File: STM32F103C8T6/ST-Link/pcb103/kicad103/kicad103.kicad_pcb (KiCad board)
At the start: 4 copper layers, 82 x 52 mm, 32 parts, among them IC1 LD1117DT33TR, J1 0480372200, J2 Conn_01x02_Socket, J3 Conn_02x05_Odd_Even, J5 Conn_01x16_Pin, J7 Conn_01x04_Pin, J8 Conn_01x05_Socket, J9 Conn_01x17_Pin, U1 STM32F103C8T6, Y1 8MHz 20pF

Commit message: Fix remaining
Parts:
- moved C6 0.80 mm to (81.6, 60.2)
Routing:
- net +3.3V: track 50.2 -> 51.9 mm
- net PA15: track 85.7 -> 87.0 mm

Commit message: Move line from top header
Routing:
- net PB11: track 65.7 -> 67.9 mm
- net PB14: track 98.2 -> 100.2 mm
- net PB13: track 88.4 -> 86.5 mm, vias 1 -> 3

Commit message: Move out bottom lines
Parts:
- moved H4 1.10 mm to (56.6, 87.0)
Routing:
- net PB0: track 115.9 -> 99.9 mm
- net PB1: track 124.3 -> 109.0 mm
- net PB2: track 122.5 -> 108.8 mm
- net PB15: track 122.3 -> 135.5 mm
- net PB10: track 128.0 -> 115.9 mm
- net PC15: track 76.8 -> 87.9 mm
- net PB11: track 67.9 -> 61.3 mm
- net PC13: track 79.3 -> 84.1 mm
- net PC14: track 38.6 -> 38.9 mm, vias 1 -> 3

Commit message: Move out mounting hole
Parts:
- removed H4: MountingHole_Pad, MountingHole:MountingHole_4.3mm_M4_Pad_Via
- moved H2 6.35 mm to (121.2, 88.2)
- moved H3 2.38 mm to (58.0, 50.6)
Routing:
- net PB10: track 115.9 -> 177.0 mm
- net PB2: track 108.8 -> 161.2 mm
- net PB1: track 109.0 -> 160.5 mm
- net PB0: track 99.9 -> 150.8 mm
- net PA1: track 24.1 -> 54.8 mm
- net PC15: track 87.9 -> 103.6 mm
- net PB15: track 135.5 -> 147.7 mm

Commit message: Clean lines from header pins
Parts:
- moved H1 7.08 mm to (121.2, 49.6)
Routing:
- net PA15: track 87.0 -> 102.2 mm
- net PB1: track 160.5 -> 154.6 mm, vias 3 -> 5
- net PB3: track 52.3 -> 47.2 mm
- net PB13: track 86.5 -> 91.4 mm
- net PB10: track 177.0 -> 172.5 mm
- net PB2: track 161.2 -> 157.1 mm
- net PB12: track 117.3 -> 120.9 mm
- net PB14: track 100.2 -> 98.8 mm
- net PA13: track 49.9 -> 51.3 mm
- net GND: track 44.2 -> 44.9 mm
- net PA14: track 61.9 -> 62.5 mm

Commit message: Add header 1 front lables
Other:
- board text added: "PA0"
- board text added: "PA1"
- board text added: "PA10"
- board text added: "PA13"
- board text added: "PA14"
- board text added: "PA15"
- board text added: "PA2"
- board text added: "PA3"
- board text added: "PA4"
- board text added: "PA5"
- board text added: "PA6"
- board text added: "PA7"
- board text added: "PA8"
- board text added: "PA9"
- board text added: "PC13"
- board text added: "PC14"
- board text added: "PC15"
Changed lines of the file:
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@@
     (effects (font (size 1 1) (thickness 0.2) bold) (justify left bottom mirror))
+  )
+  (gr_text "PC14" (at 105 92.9 90) (layer "F.SilkS")
+    (effects (font (size 1 1) (thickness 0.2) bold) (justify left bottom))
   )
   (gr_text "1" (at 95.1 59.5) (layer "F.SilkS")
@@
     (effects (font (size 1 1) (thickness 0.2) bold) (justify left bottom))
   )
+  (gr_text "PA13" (at 94.8 92.9 90) (layer "F.SilkS")
+    (effects (font (size 1 1) (thickness 0.2) bold) (justify left bottom))
+  )
+  (gr_text "PA1" (at 69.3 91.8 90) (layer "F.SilkS")
+    (effects (font (size 1 1) (thickness 0.2) bold) (justify left bottom))
+  )
   (gr_text "JTAG" (at 98.7 57.6) (layer "F.SilkS")
+    (effects (font (size 1 1) (thickness 0.2) bold) (justify left bottom))
+  )
+  (gr_text "PA5" (at 79.6 91.8 90) (layer "F.SilkS")
     (effects (font (size 1 1) (thickness 0.2) bold) (justify left bottom))
   )
@@
     (effects (font (size 1 1) (thickness 0.2) bold) (justify left bottom))
   )
+  (gr_text "PA2" (at 71.9 91.8 90) (layer "F.SilkS")
+    (effects (font (size 1 1) (thickness 0.2) bold) (justify left bottom))
+  )
   (gr_text "SWDIO" (at 110.5 64.3) (layer "F.SilkS")
     (effects (font (size 1 1) (thickness 0.2) bold) (justify left bottom))
   )
+  (gr_text "PC15" (at 107.5 92.9 90) (layer "F.SilkS")
+    (effects (font (size 1 1) (thickness 0.2) bold) (justify left bottom))
+  )
+  (gr_text "PA15" (at 99.9 92.9 90) (layer "F.SilkS")
+    (effects (font (size 1 1) (thickness 0.2) bold) (justify left bottom))
+  )
+  (gr_text "PA8" (at 87.2 91.8 90) (layer "F.SilkS")
+    (effects (font (size 1 1) (thickness 0.2) bold) (justify left bottom))
+  )
   (gr_text "SWCLK" (at 110.5 67) (layer "F.SilkS")
+    (effects (font (size 1 1) (thickness 0.2) bold) (justify left bottom))
+  )
+  (gr_text "PA0" (at 66.8 91.8 90) (layer "F.SilkS")
+    (effects (font (size 1 1) (thickness 0.2) bold) (justify left bottom))
+  )
+  (gr_text "1" (at 78.5 65.7) (layer "F.SilkS")
+    (effects (font (size 1 1) (thickness 0.2) bold) (justify left bottom))
+  )
+  (gr_text "PA4" (at 77 91.8 90) (layer "F.SilkS")
+    (effects (font (size 1 1) (thickness 0.2) bold) (justify left bottom))
+  )
+  (gr_text "PA10" (at 92.2 92.9 90) (layer "F.SilkS")
     (effects (font (size 1 1) (thickness 0.2) bold) (justify left bottom))
   )
@@
   )
   (gr_text "+" (at 64.2 76.1) (layer "F.SilkS")
+    (effects (font (size 1 1) (thickness 0.2) bold) (justify left bottom))
+  )
+  (gr_text "PA9" (at 89.7 91.8 90) (layer "F.SilkS")
+    (effects (font (size 1 1) (thickness 0.2) bold) (justify left bottom))
+  )
+  (gr_text "PA7" (at 84.7 91.8 90) (layer "F.SilkS")
+    (effects (font (size 1 1) (thickness 0.2) bold) (justify left bottom))
+  )
+  (gr_text "PA14" (at 97.3 92.9 90) (layer "F.SilkS")
+    (effects (font (size 1 1) (thickness 0.2) bold) (justify left bottom))
+  )
+  (gr_text "PA3" (at 74.4 91.8 90) (layer "F.SilkS")
     (effects (font (size 1 1) (thickness 0.2) bold) (justify left bottom))
   )
@@
     (effects (font (size 1 1) (thickness 0.2) bold) (justify left bottom))
   )
+  (gr_text "PC13" (at 102.4 92.9 90) (layer "F.SilkS")
+    (effects (font (size 1 1) (thickness 0.2) bold) (justify left bottom))
+  )
+  (gr_text "PA6" (at 82.2 91.8 90) (layer "F.SilkS")
+    (effects (font (size 1 1) (thickness 0.2) bold) (justify left bottom))
+  )

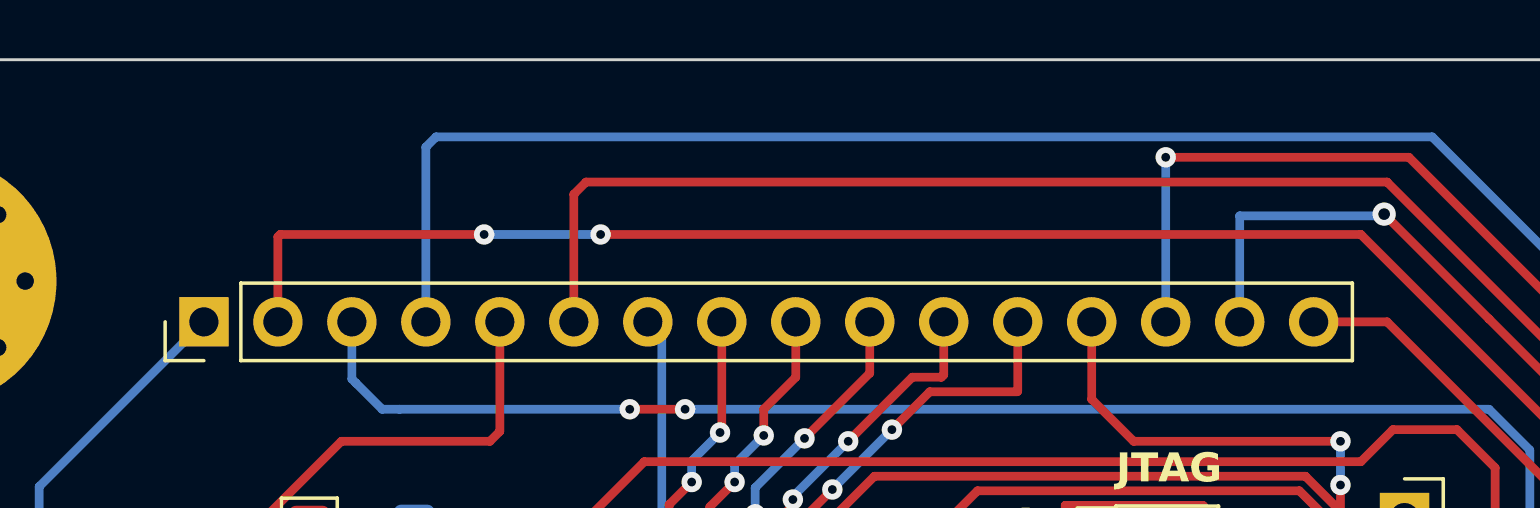
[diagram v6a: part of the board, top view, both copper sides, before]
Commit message: Add header 1 back lables
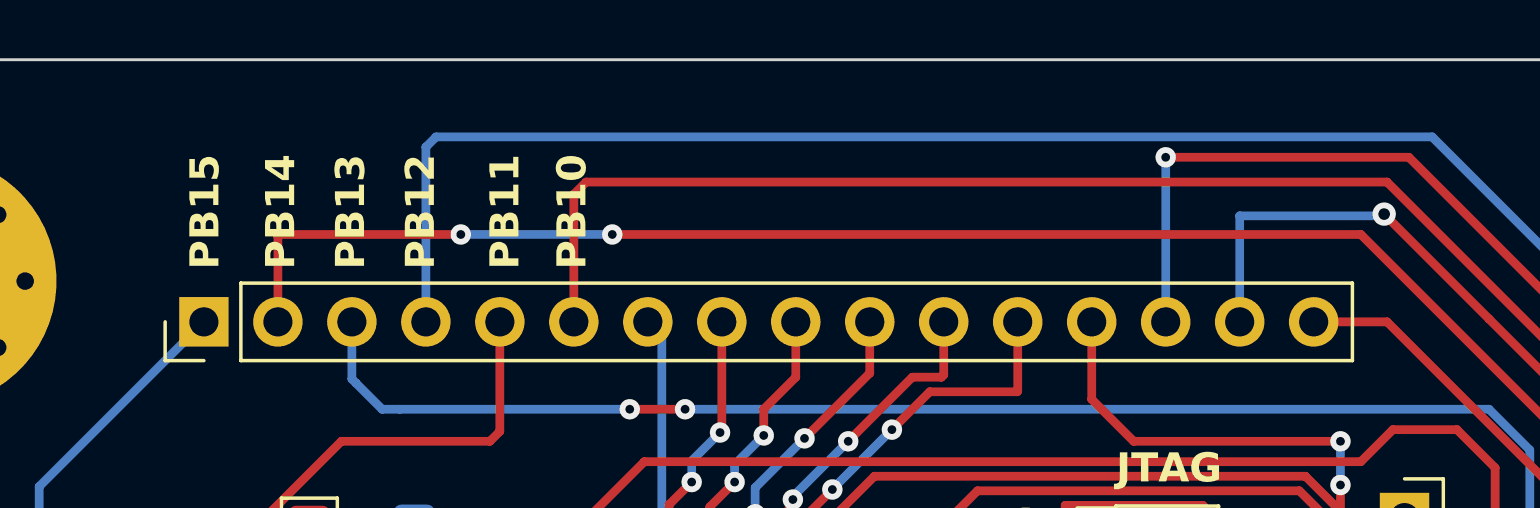
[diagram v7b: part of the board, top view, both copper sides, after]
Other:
- board text added: "PB10"
- board text added: "PB11"
- board text added: "PB12"
- board text added: "PB13"
- board text added: "PB14"
- board text added: "PB15"
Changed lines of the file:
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@@
   (gr_line (start 124 43) (end 58 43)
     (stroke (width 0.1) (type default)) (layer "Edge.Cuts"))
+  (gr_text "PA2" (at 72 89.2 90) (layer "B.SilkS")
+    (effects (font (size 1 1) (thickness 0.2) bold) (justify left bottom mirror))
+  )
   (gr_text "GND" (at 113.7 69.5) (layer "B.SilkS")
     (effects (font (size 1 1) (thickness 0.2) bold) (justify left bottom mirror))
@@
     (effects (font (size 1 1) (thickness 0.2) bold) (justify left bottom mirror))
   )
+  (gr_text "PA14" (at 97.4 89.2 90) (layer "B.SilkS")
+    (effects (font (size 1 1) (thickness 0.2) bold) (justify left bottom mirror))
+  )
+  (gr_text "PA9" (at 89.8 89.2 90) (layer "B.SilkS")
+    (effects (font (size 1 1) (thickness 0.2) bold) (justify left bottom mirror))
+  )
+  (gr_text "PA4" (at 77.1 89.2 90) (layer "B.SilkS")
+    (effects (font (size 1 1) (thickness 0.2) bold) (justify left bottom mirror))
+  )
   (gr_text "PWR" (at 60.1 81.2) (layer "B.SilkS")
     (effects (font (size 1 1) (thickness 0.2) bold) (justify left bottom mirror))
   )
+  (gr_text "PA13" (at 94.8 89.2 90) (layer "B.SilkS")
+    (effects (font (size 1 1) (thickness 0.2) bold) (justify left bottom mirror))
+  )
+  (gr_text "PA10" (at 92.3 89.2 90) (layer "B.SilkS")
+    (effects (font (size 1 1) (thickness 0.2) bold) (justify left bottom mirror))
+  )
   (gr_text "SWDIO" (at 115.3 64.3) (layer "B.SilkS")
     (effects (font (size 1 1) (thickness 0.2) bold) (justify left bottom mirror))
@@
     (effects (font (size 1 1) (thickness 0.2) bold) (justify left bottom mirror))
   )
+  (gr_text "PA15" (at 99.9 89.2 90) (layer "B.SilkS")
+    (effects (font (size 1 1) (thickness 0.2) bold) (justify left bottom mirror))
+  )
+  (gr_text "PA6" (at 82.1 89.2 90) (layer "B.SilkS")
+    (effects (font (size 1 1) (thickness 0.2) bold) (justify left bottom mirror))
+  )
   (gr_text "SWCLK" (at 121 76.9) (layer "B.SilkS")
     (effects (font (size 1 1) (thickness 0.2) bold) (justify left bottom mirror))
   )
+  (gr_text "PC13" (at 102.5 89.2 90) (layer "B.SilkS")
+    (effects (font (size 1 1) (thickness 0.2) bold) (justify left bottom mirror))
+  )
+  (gr_text "PC14" (at 105 89.2 90) (layer "B.SilkS")
+    (effects (font (size 1 1) (thickness 0.2) bold) (justify left bottom mirror))
+  )
+  (gr_text "PA0" (at 66.8 89.2 90) (layer "B.SilkS")
+    (effects (font (size 1 1) (thickness 0.2) bold) (justify left bottom mirror))
+  )
   (gr_text "3.3V" (at 115.1 61.9) (layer "B.SilkS")
     (effects (font (size 1 1) (thickness 0.2) bold) (justify left bottom mirror))
@@
     (effects (font (size 1 1) (thickness 0.2) bold) (justify left bottom mirror))
   )
+  (gr_text "PA1" (at 69.4 89.2 90) (layer "B.SilkS")
+    (effects (font (size 1 1) (thickness 0.2) bold) (justify left bottom mirror))
+  )
+  (gr_text "PA3" (at 74.5 89.2 90) (layer "B.SilkS")
+    (effects (font (size 1 1) (thickness 0.2) bold) (justify left bottom mirror))
+  )
+  (gr_text "PA8" (at 87.2 89.2 90) (layer "B.SilkS")
+    (effects (font (size 1 1) (thickness 0.2) bold) (justify left bottom mirror))
+  )
   (gr_text "Slave" (at 106.6 61.8 90) (layer "B.SilkS")
     (effects (font (size 1 1) (thickness 0.2) bold) (justify left bottom mirror))
   )
+  (gr_text "PA5" (at 79.6 89.2 90) (layer "B.SilkS")
+    (effects (font (size 1 1) (thickness 0.2) bold) (justify left bottom mirror))
+  )
+  (gr_text "PC15" (at 107.5 89.2 90) (layer "B.SilkS")
+    (effects (font (size 1 1) (thickness 0.2) bold) (justify left bottom mirror))
+  )
   (gr_text "-" (at 62.8 78.5) (layer "B.SilkS")
     (effects (font (size 1 1) (thickness 0.2) bold) (justify left bottom mirror))
   )
+  (gr_text "PA7" (at 84.7 89.2 90) (layer "B.SilkS")
+    (effects (font (size 1 1) (thickness 0.2) bold) (justify left bottom mirror))
+  )
   (gr_text "3.3V" (at 119.3 71.9) (layer "B.SilkS")
     (effects (font (size 1 1) (thickness 0.2) bold) (justify left bottom mirror))
@@
     (effects (font (size 1 1) (thickness 0.2) bold) (justify left bottom))
   )
+  (gr_text "PB14" (at 70.6 50.2 90) (layer "F.SilkS")
+    (effects (font (size 1 1) (thickness 0.2) bold) (justify left bottom))
+  )
   (gr_text "PA13" (at 94.8 92.9 90) (layer "F.SilkS")
     (effects (font (size 1 1) (thickness 0.2) bold) (justify left bottom))
@@
     (effects (font (size 1 1) (thickness 0.2) bold) (justify left bottom))
   )
+  (gr_text "PB10" (at 80.6 50.2 90) (layer "F.SilkS")
+    (effects (font (size 1 1) (thickness 0.2) bold) (justify left bottom))
+  )
   (gr_text "SWCLK" (at 110.5 67) (layer "F.SilkS")
     (effects (font (size 1 1) (thickness 0.2) bold) (justify left bottom))
@@
     (effects (font (size 1 1) (thickness 0.2) bold) (justify left bottom))
   )
+  (gr_text "PB13" (at 73 50.2 90) (layer "F.SilkS")
+    (effects (font (size 1 1) (thickness 0.2) bold) (justify left bottom))
+  )
   (gr_text "PA14" (at 97.3 92.9 90) (layer "F.SilkS")
     (effects (font (size 1 1) (thickness 0.2) bold) (justify left bottom))
@@
     (effects (font (size 1 1) (thickness 0.2) bold) (justify left bottom))
   )
+  (gr_text "PB15" (at 68 50.2 90) (layer "F.SilkS")
+    (effects (font (size 1 1) (thickness 0.2) bold) (justify left bottom))
+  )
   (gr_text "3.3V" (at 111.5 61.9) (layer "F.SilkS")
     (effects (font (size 1 1) (thickness 0.2) bold) (justify left bottom))
@@
     (effects (font (size 1 1) (thickness 0.2) bold) (justify left bottom))
   )
+  (gr_text "PB12" (at 75.4 50.2 90) (layer "F.SilkS")
+    (effects (font (size 1 1) (thickness 0.2) bold) (justify left bottom))
+  )
   (gr_text "PC13" (at 102.4 92.9 90) (layer "F.SilkS")
+    (effects (font (size 1 1) (thickness 0.2) bold) (justify left bottom))
+  )
+  (gr_text "PB11" (at 78.3 50.2 90) (layer "F.SilkS")
     (effects (font (size 1 1) (thickness 0.2) bold) (justify left bottom))
   )
@@
   (segment (start 91 68.8) (end 91 71.6) (width 0.3) (layer "B.Cu") (net 19))
   (segment (start 61.6 81.71005) (end 65.352082 77.957968) (width 0.3) (layer "B.Cu") (net 19))
-  (segment (start 107.1 49) (end 81 49) (width 0.3) (layer "F.Cu") (net 20))
+  (segment (start 118.7 70.3) (end 118.7 61.7) (width 0.3) (layer "F.Cu") (net 20))
   (segment (start 102.2625 69.9) (end 105.9 73.5375) (width 0.3) (layer "F.Cu") (net 20))
-  (segment (start 114.7 56.6) (end 107.1 49) (width 0.3) (layer "F.Cu") (net 20))
   (segment (start 114 73.62) (end 105.9825 73.62) (width 0.3) (layer "F.Cu") (net 20))
+  (segment (start 70 49) (end 76.2 49) (width 0.3) (layer "F.Cu") (net 20))
   (segment (start 69.92 49.08) (end 69.92 52) (width 0.3) (layer "F.Cu") (net 20))
   (segment (start 70 49) (end 69.92 49.08) (width 0.3) (layer "F.Cu") (net 20))
+  (segment (start 114.7 56.6) (end 107.1 49) (width 0.3) (layer "F.Cu") (net 20))
   (segment (start 105.9825 73.62) (end 105.9 73.5375) (width 0.3) (layer "F.Cu") (net 20))
   (segment (start 115.38 73.62) (end 118.7 70.3) (width 0.3) (layer "F.Cu") (net 20))
+  (segment (start 107.1 49) (end 81.4 49) (width 0.3) (layer "F.Cu") (net 20))
+  (segment (start 114 73.62) (end 115.38 73.62) (width 0.3) (layer "F.Cu") (net 20))
   (segment (start 118.7 61.7) (end 114.7 57.7) (width 0.3) (layer "F.Cu") (net 20))
   (segment (start 114.7 57.7) (end 114.7 56.6) (width 0.3) (layer "F.Cu") (net 20))
   (segment (start 106.0025 73.64) (end 105.9 73.5375) (width 0.5) (layer "F.Cu") (net 20))
-  (segment (start 77 49) (end 70 49) (width 0.3) (layer "F.Cu") (net 20))
-  (segment (start 118.7 70.3) (end 118.7 61.7) (width 0.3) (layer "F.Cu") (net 20))
   (segment (start 89.1625 69.9) (end 102.2625 69.9) (width 0.3) (layer "F.Cu") (net 20))
-  (segment (start 114 73.62) (end 115.38 73.62) (width 0.3) (layer "F.Cu") (net 20))
-  (via (at 77 49) (size 0.7) (drill 0.3) (layers "F.Cu" "B.Cu") (net 20))
-  (via (at 81 49) (size 0.7) (drill 0.3) (layers "F.Cu" "B.Cu") (net 20))
-  (segment (start 81 49) (end 77 49) (width 0.3) (layer "B.Cu") (net 20))
+  (via (at 76.2 49) (size 0.7) (drill 0.3) (layers "F.Cu" "B.Cu") (net 20))
+  (via (at 81.4 49) (size 0.7) (drill 0.3) (layers "F.Cu" "B.Cu") (net 20))
+  (segment (start 81.4 49) (end 76.2 49) (width 0.3) (layer "B.Cu") (net 20))
   (segment (start 109 75.55) (end 103.55 75.55) (width 0.3) (layer "F.Cu") (net 21))
   (segment (start 113.39 75.55) (end 109 75.55) (width 0.3) (layer "F.Cu") (net 21))

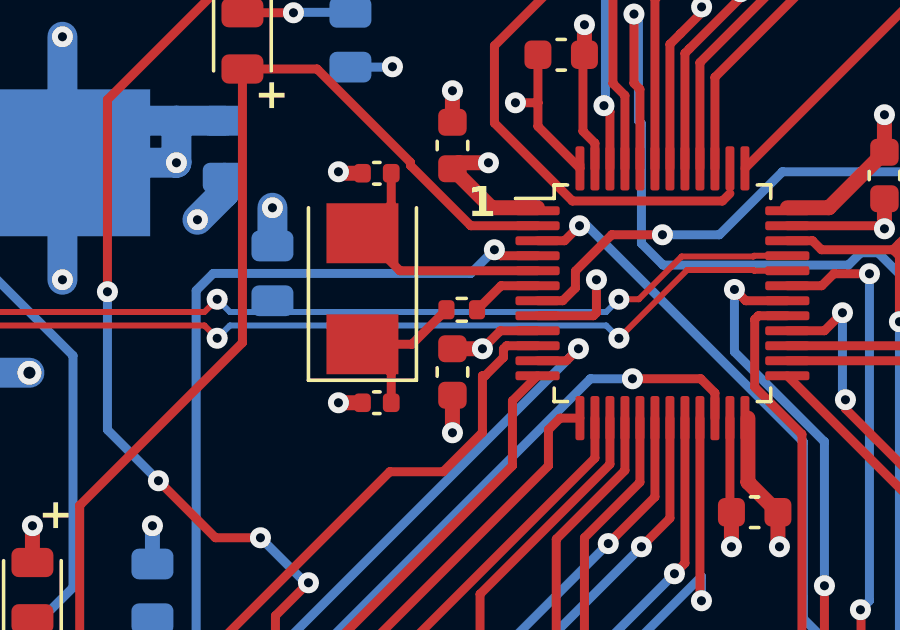
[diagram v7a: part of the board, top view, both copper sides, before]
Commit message: Move crystal resistor
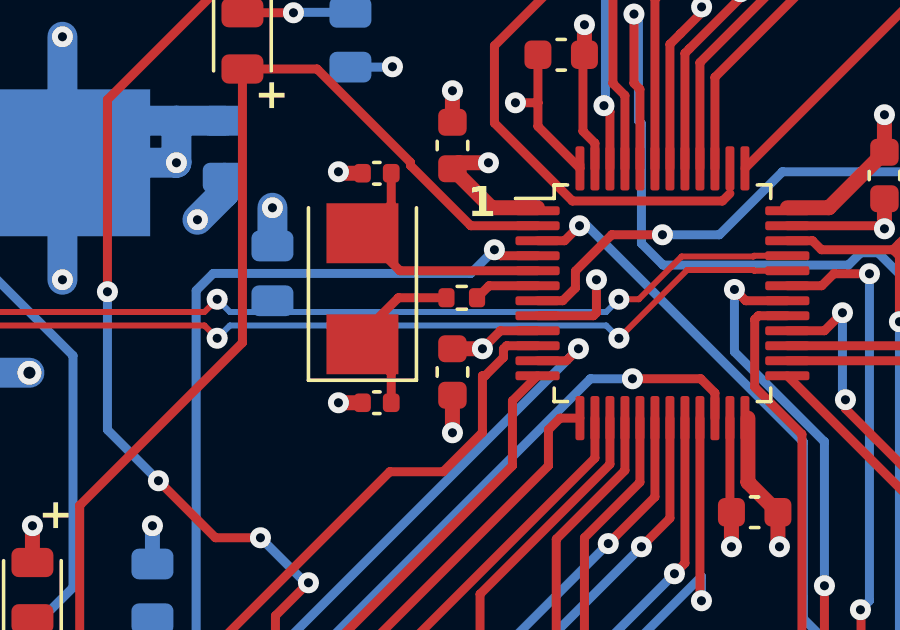
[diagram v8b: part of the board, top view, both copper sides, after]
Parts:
- moved R3 0.40 mm to (78.3, 68.3)
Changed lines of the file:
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@@
   )
   (footprint "Resistor_SMD:R_0402_1005Metric" (layer "F.Cu")
-    (at 78.31 68.7)
+    (at 78.31 68.3)
     (descr "Resistor SMD 0402 (1005 Metric), square (rectangular) end terminal, IPC_7351 nominal, (Body size source: IPC-SM-782 page 72, https://www.pcb-3d.com/wordpress/wp-content/uploads/ipc-sm-782a_amendment_1_and_2.pdf), generated with kicad-footprint-generator")
     (tags "resistor")
@@
   (segment (start 75.96 64.15) (end 75.96 65.19) (width 0.3) (layer "F.Cu") (net 12))
   (segment (start 80.8375 67.4) (end 76.25 67.4) (width 0.3) (layer "F.Cu") (net 12))
-  (segment (start 77.8 68.7) (end 76.65 69.85) (width 0.3) (layer "F.Cu") (net 13))
+  (segment (start 76.2 68.3) (end 77.8 68.3) (width 0.3) (layer "F.Cu") (net 13))
   (segment (start 75.96 71.8) (end 75.96 70.81) (width 0.3) (layer "F.Cu") (net 13))
+  (segment (start 75 69.85) (end 75 69.5) (width 0.3) (layer "F.Cu") (net 13))
   (segment (start 75.96 70.81) (end 75 69.85) (width 0.3) (layer "F.Cu") (net 13))
-  (segment (start 76.65 69.85) (end 75 69.85) (width 0.3) (layer "F.Cu") (net 13))
+  (segment (start 75 69.5) (end 76.2 68.3) (width 0.3) (layer "F.Cu") (net 13))
   (segment (start 93.9375 57.8) (end 87.75 63.9875) (width 0.3) (layer "F.Cu") (net 14))
   (segment (start 104.89995 60.29) (end 105.9 59.28995) (width 0.3) (layer "F.Cu") (net 14))
@@
   (segment (start 91.9 67.5) (end 91.9 78.4) (width 0.3) (layer "B.Cu") (net 47))
   (segment (start 91.9 78.4) (end 91.6 78.7) (width 0.3) (layer "B.Cu") (net 47))
-  (segment (start 79.62 67.9) (end 78.82 68.7) (width 0.3) (layer "F.Cu") (net 48))
-  (segment (start 80.8375 67.9) (end 79.62 67.9) (width 0.3) (layer "F.Cu") (net 48))
+  (segment (start 79.22 67.9) (end 78.82 68.3) (width 0.3) (layer "F.Cu") (net 48))
+  (segment (start 80.8375 67.9) (end 79.22 67.9) (width 0.3) (layer "F.Cu") (net 48))
   (segment (start 80.8375 68.4) (end 81.676041 68.4) (width 0.3) (layer "F.Cu") (net 49))
   (segment (start 82.1 67.976041) (end 82.1 67.41005) (width 0.3) (layer "F.Cu") (net 49))
